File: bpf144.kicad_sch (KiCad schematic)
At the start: 39 parts

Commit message: 部品定数を入力　ただし未評価
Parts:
- C301, C330: value 10p -> NM
- C302, C329: value 10p -> 1000p
- C303, C305, C307, C309, C311, C313, C315, C317, C319, C321, C323, C325, C327: value 1p -> NM
- C304, C328: value 10p -> 47p
- C306, C320: value 10p -> 100p
- C310, C326: value 10p -> 68p
- C314: value 10p -> 22p
- C318: value 10p -> 33p
- L303, L305: value 10n -> NM
- L304, L306: value 1u -> 10n
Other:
- note added: "2t D3.5mm L3.2mm"
- note added: "Butterworth 134M-156M 26.7p, 13.1p, 98.6p"
- company: (none) -> JK1MLY / PRUG
- title: (none) -> FM QRP TRCV

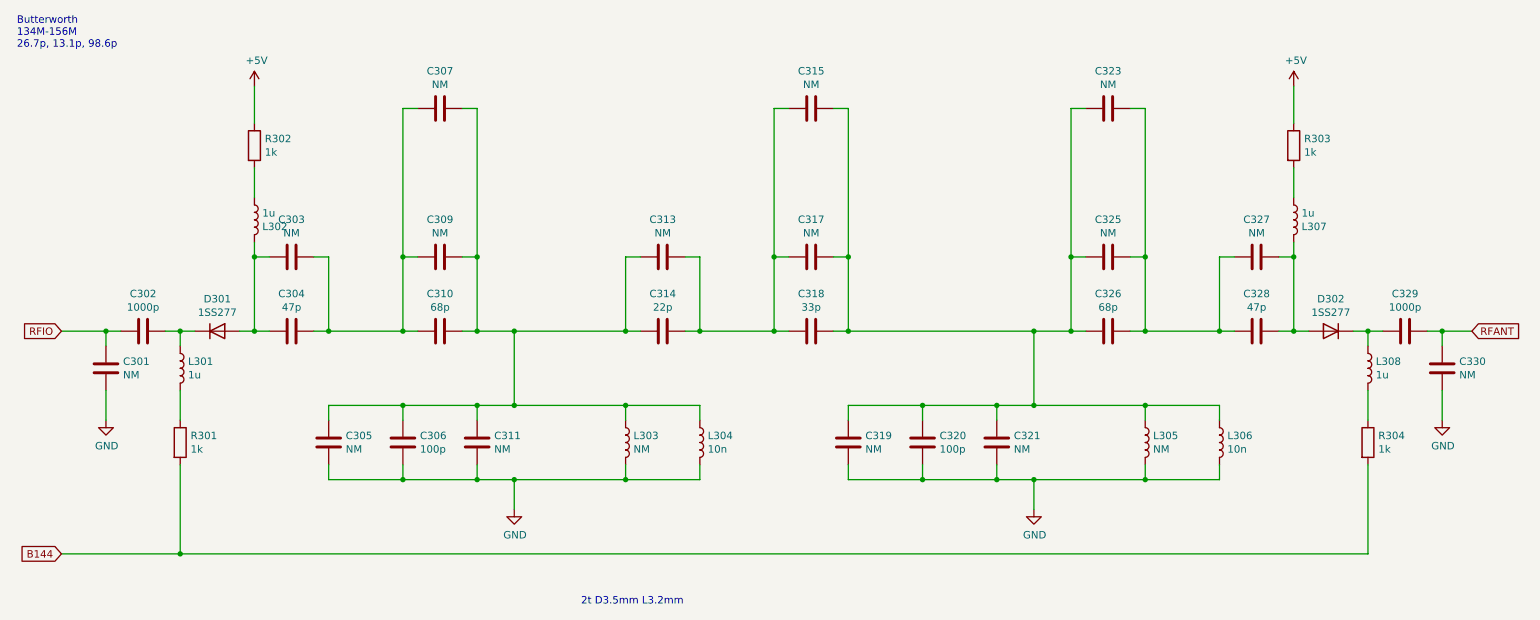
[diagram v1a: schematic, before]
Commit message: バンドパスフィルタの定数を見直し（単体試験の反映）
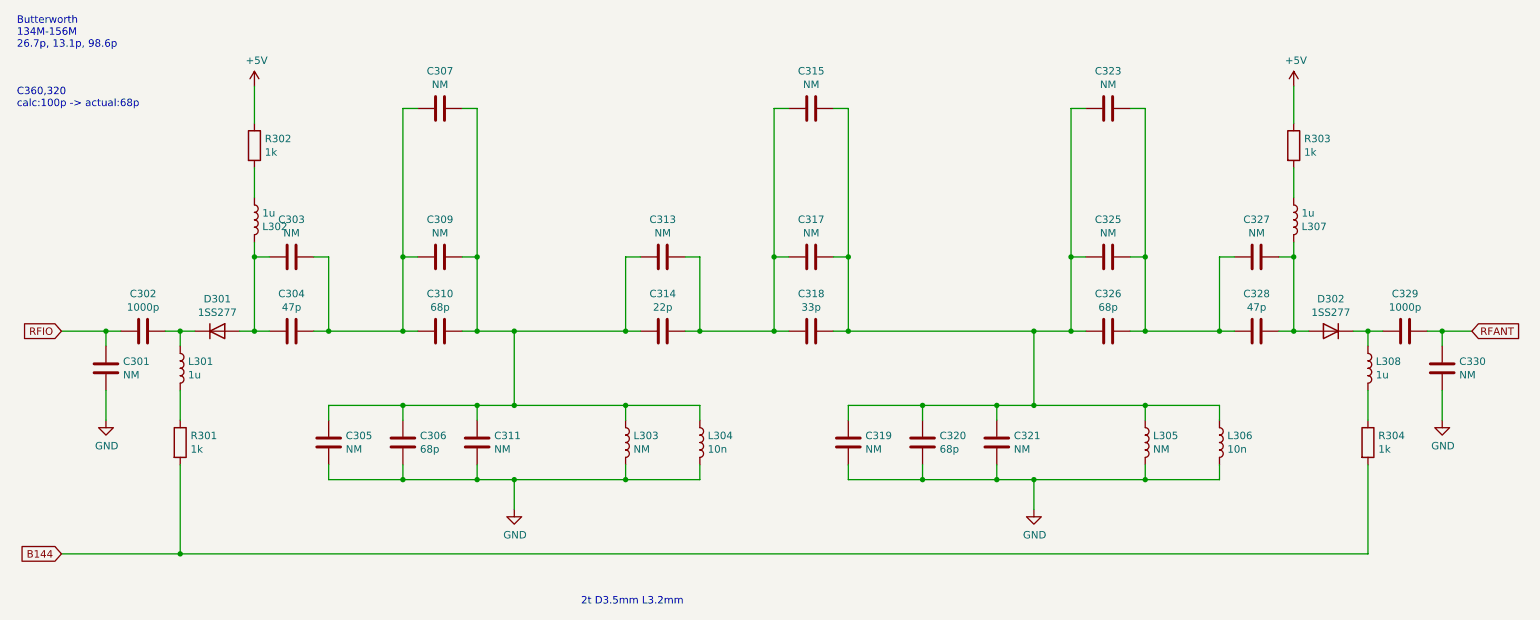
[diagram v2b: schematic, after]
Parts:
- C306, C320: value 100p -> 68p
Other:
- note added: "C360,320 calc:100p -> actual:68p"
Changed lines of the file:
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@@
+    (effects (font (size 1.27 1.27)) (justify left bottom))
+  )
+  (text "C360,320\ncalc:100p -> actual:68p" (at 22.86 38.1 0)
     (effects (font (size 1.27 1.27)) (justify left bottom))
   )
@@
       (effects (font (size 1.27 1.27)) (justify left))
     )
-    (property "Value" "100p" (id 1) (at 180.721 96.393 0)
+    (property "Value" "68p" (id 1) (at 180.721 96.393 0)
       (effects (font (size 1.27 1.27)) (justify left))
     )
@@
       (effects (font (size 1.27 1.27)) (justify left))
     )
-    (property "Value" "100p" (id 1) (at 91.821 96.393 0)
-      (effects (font (size 1.27 1.27)) (justify left))
-    )
+    (property "Value" "68p" (id 1) (at 91.821 96.393 0)
+      (effects (font (size 1.27 1.27)) (justify left))
+    )

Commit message: Add files via upload
フィルタ回路変更とジャンパクリーン
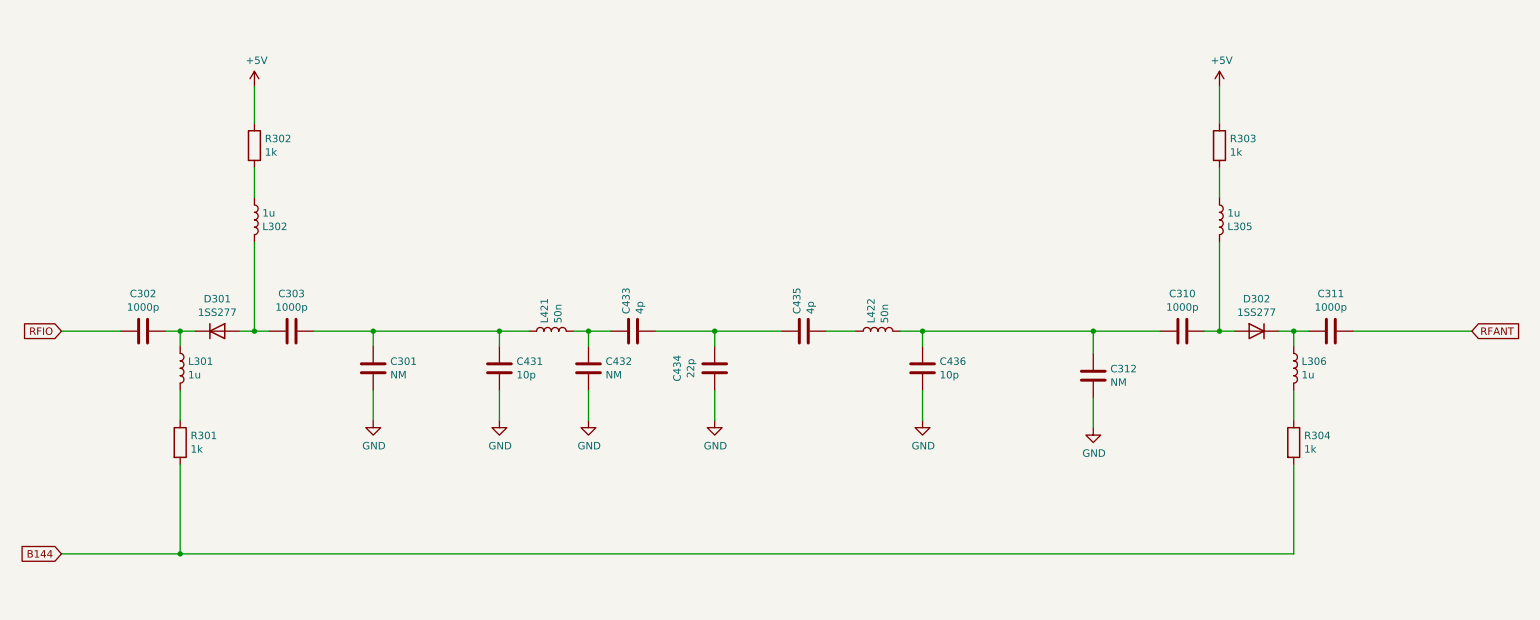
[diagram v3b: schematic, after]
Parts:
- removed C303, C305, C307, C309, C311, C313, C315, C317, C319, C321, C323, C325, C327: NM, digikey-footprints:0603, symbol Device:C
- removed C306, C310, C320, C326: 68p, Capacitor_THT:C_Disc_D3.4mm_W2.1mm_P2.50mm, symbol Device:C
- removed C314: 22p, Capacitor_THT:C_Disc_D3.4mm_W2.1mm_P2.50mm, symbol Device:C
- removed C318: 33p, Capacitor_THT:C_Disc_D3.4mm_W2.1mm_P2.50mm, symbol Device:C
- removed L303, L305: NM, Inductor_SMD:L_Murata_LQH2MCNxxxx02_2.0x1.6mm, symbol Device:L
- removed L304, L306: 10n, Resistor_THT:R_Axial_DIN0204_L3.6mm_D1.6mm_P5.08mm_Horizontal, symbol Device:L
- added C431, C436: 10p, Capacitor_THT:C_Disc_D3.4mm_W2.1mm_P2.50mm, symbol Device:C
- added C432: NM, Capacitor_THT:C_Disc_D3.4mm_W2.1mm_P2.50mm, symbol Device:C
- added C433, C435: 4p, Capacitor_THT:C_Disc_D3.4mm_W2.1mm_P2.50mm, symbol Device:C
- added C434: 22p, Capacitor_THT:C_Disc_D3.4mm_W2.1mm_P2.50mm, symbol Device:C
- added L421, L422: 50n, usr-Library:coil3_7mm, symbol Device:L
- C303: renamed from C304; value 47p -> 1000p
- C310: renamed from C328; value 47p -> 1000p
- renumbered C329 to C311, C330 to C312, L307 to L305, L308 to L306
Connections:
- net GND: now also C431.2, C432.2, C434.1, C436.2
- net RFANT: no longer C312.1
- net RFIO: no longer C301.1
- net at C303.2: now also C301.1, C431.1, L421.1
- net at C310.1: now also C312.1, C436.1, L422.2
- new net: C432.1, C433.1, L421.2
- new net: C433.2, C434.2, C435.1
- new net: C435.2, L422.1
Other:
- note removed: "2t D3.5mm L3.2mm"
- note removed: "Butterworth 134M-156M 26.7p, 13.1p, 98.6p"
- note removed: "C360,320 calc:100p -> actual:68p"
- moved on the sheet: C301, C310, C311, C312, D302, L305, L306, R303, R304

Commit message: アップデート
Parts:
- removed C301, C312: NM, Capacitor_THT:C_Disc_D3.4mm_W2.1mm_P2.50mm, symbol Device:C
- removed C435: 4p, Capacitor_THT:C_Disc_D3.4mm_W2.1mm_P2.50mm, symbol Device:C
- added R102: 1k, Resistor_THT:R_Axial_DIN0207_L6.3mm_D2.5mm_P2.54mm_Vertical, symbol Device:R
- C431, C436: value 10p -> 15p
- C432: value NM -> 15p
- C433: value 4p -> 33p
- C434: value 22p -> 15p
- D301, D302: footprint Diode_THT:D_A-405_P2.54mm_Vertical_AnodeUp -> Diode_THT:D_T-1_P5.08mm_Horizontal
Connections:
- net +5V: now also R102.1
- net B144: now also R102.2
- net at C433.2, C434.2: now also L422.1

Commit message: Add files via upload
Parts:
- C302, C303, C310, C311: value 1000p -> 0.01u
- L301, L302, L305, L306: value 1u -> 10u
- L421, L422: value 50n -> 60n
- R301, R302, R303, R304: value 1k -> 470
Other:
- note added: "L303,304は5mm 4.5T corecraft 164-04A06L相当 コアをトップと同じか半回転上にしたあたり 以前はaitendoで入手できたが現在は不可"
- note added: "注 C302 シルク無"
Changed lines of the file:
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@@
   (title_block
     (title "FM QRP TRCV")
-    (date "2022-03-12")
+    (date "2023-08-12")
     (rev "1")
     (company "JK1MLY / PRUG")
@@
   (wire (pts (xy 177.8 76.2) (xy 218.44 76.2))
     (stroke (width 0) (type default))
+  )
+  (text "注　C302 シルク無" (at 36.83 63.5 0)
+    (effects (font (size 1.27 1.27)) (justify left bottom))
+  )
+  (text "L303,304は5mm 4.5T\ncorecraft 164-04A06L相当\nコアをトップと同じか半回転上にしたあたり\n以前はaitendoで入手できたが現在は不可"
+    (at 106.68 59.69 0)
+    (effects (font (size 1.27 1.27)) (justify left bottom))
   )
   (global_label "RFANT" (shape input) (at 271.78 76.2 0) (fields_autoplaced)
@@
       (effects (font (size 1.27 1.27)) (justify left))
     )
-    (property "Value" "1u" (at 242.6462 83.693 0)
+    (property "Value" "10u" (at 242.6462 83.693 0)
       (effects (font (size 1.27 1.27)) (justify left))
     )
@@
       (effects (font (size 1.27 1.27)) (justify left))
     )
-    (property "Value" "1k" (at 65.278 45.593 0)
+    (property "Value" "470" (at 65.278 45.593 0)
       (effects (font (size 1.27 1.27)) (justify left))
     )
@@
       (effects (font (size 1.27 1.27)) hide)
     )
-    (property "Datasheet" "~" (at 63.5 44.45 0)
+    (property "Datasheet" "R-25471" (at 63.5 44.45 0)
       (effects (font (size 1.27 1.27)) hide)
     )
@@
       (effects (font (size 1.27 1.27)) (justify left))
     )
-    (property "Value" "1k" (at 243.078 96.393 0)
+    (property "Value" "470" (at 243.078 96.393 0)
       (effects (font (size 1.27 1.27)) (justify left))
     )
@@
       (effects (font (size 1.27 1.27)) hide)
     )
-    (property "Datasheet" "~" (at 241.3 95.25 0)
+    (property "Datasheet" "R-25471" (at 241.3 95.25 0)
       (effects (font (size 1.27 1.27)) hide)
     )
@@
       (effects (font (size 1.27 1.27)))
     )
-    (property "Value" "1000p" (at 69.85 72.1106 90)
+    (property "Value" "0.01u" (at 69.85 72.1106 90)
       (effects (font (size 1.27 1.27)))
     )
@@
       (effects (font (size 1.27 1.27)) hide)
     )
-    (property "Datasheet" "~" (at 69.85 76.2 0)
+    (property "Datasheet" "sato" (at 69.85 76.2 0)
       (effects (font (size 1.27 1.27)) hide)
     )
@@
       (effects (font (size 1.27 1.27)))
     )
-    (property "Value" "1000p" (at 222.25 72.1106 90)
+    (property "Value" "0.01u" (at 222.25 72.1106 90)
       (effects (font (size 1.27 1.27)))
     )
@@
       (effects (font (size 1.27 1.27)) hide)
     )
-    (property "Datasheet" "~" (at 222.25 76.2 0)
+    (property "Datasheet" "sato" (at 222.25 76.2 0)
       (effects (font (size 1.27 1.27)) hide)
     )
@@
       (effects (font (size 1.27 1.27)) (justify left))
     )
-    (property "Value" "1u" (at 52.1462 83.693 0)
+    (property "Value" "10u" (at 52.1462 83.693 0)
       (effects (font (size 1.27 1.27)) (justify left))
     )
@@
       (effects (font (size 1.27 1.27)) (justify left))
     )
-    (property "Value" "1k" (at 52.578 96.393 0)
+    (property "Value" "470" (at 52.578 96.393 0)
       (effects (font (size 1.27 1.27)) (justify left))
     )
@@
       (effects (font (size 1.27 1.27)) hide)
     )
-    (property "Datasheet" "~" (at 50.8 95.25 0)
+    (property "Datasheet" "R-25471" (at 50.8 95.25 0)
       (effects (font (size 1.27 1.27)) hide)
     )
@@
       (effects (font (size 1.27 1.27)) (justify left))
     )
-    (property "Value" "1u" (at 64.8462 56.007 0)
+    (property "Value" "10u" (at 64.8462 56.007 0)
       (effects (font (size 1.27 1.27)) (justify left))
     )
@@
       (effects (font (size 1.27 1.27)) (justify left))
     )
-    (property "Value" "1k" (at 230.378 45.593 0)
+    (property "Value" "470" (at 230.378 45.593 0)
       (effects (font (size 1.27 1.27)) (justify left))
     )
@@
       (effects (font (size 1.27 1.27)) hide)
     )
-    (property "Datasheet" "~" (at 228.6 44.45 0)
+    (property "Datasheet" "R-25471" (at 228.6 44.45 0)
       (effects (font (size 1.27 1.27)) hide)
     )
@@
       (effects (font (size 1.27 1.27)) (justify left))
     )
-    (property "Value" "1u" (at 229.9462 56.007 0)
+    (property "Value" "10u" (at 229.9462 56.007 0)
       (effects (font (size 1.27 1.27)) (justify left))
     )
@@
       (effects (font (size 1.27 1.27)))
     )
-    (property "Value" "1000p" (at 247.65 72.1106 90)
+    (property "Value" "0.01u" (at 247.65 72.1106 90)
       (effects (font (size 1.27 1.27)))
     )
@@
       (effects (font (size 1.27 1.27)) hide)
     )
-    (property "Datasheet" "~" (at 247.65 76.2 0)
+    (property "Datasheet" "sato" (at 247.65 76.2 0)
       (effects (font (size 1.27 1.27)) hide)
     )
@@
       (effects (font (size 1.27 1.27)))
     )
-    (property "Value" "1000p" (at 44.45 72.1106 90)
+    (property "Value" "0.01u" (at 44.45 72.1106 90)
       (effects (font (size 1.27 1.27)))
     )
@@
       (effects (font (size 1.27 1.27)) hide)
     )
-    (property "Datasheet" "~" (at 44.45 76.2 0)
+    (property "Datasheet" "sato" (at 44.45 76.2 0)
       (effects (font (size 1.27 1.27)) hide)
     )
@@
       (effects (font (size 1.27 1.27)) (justify left))
     )
-    (property "Value" "50n" (at 115.443 74.8538 0)
+    (property "Value" "60n" (at 115.443 74.8538 0)
       (effects (font (size 1.27 1.27)) (justify left))
     )
@@
       (effects (font (size 1.27 1.27)) hide)
     )
-    (property "Datasheet" "digikey 0805CS-3N3EJTS" (at 114.3 76.2 0)
+    (property "Datasheet" "aitendo" (at 114.3 76.2 0)
       (effects (font (size 1.27 1.27)) hide)
     )
@@
       (effects (font (size 1.27 1.27)) hide)
     )
-    (property "Datasheet" "~" (at 105.41 82.55 0)
+    (property "Datasheet" "sato" (at 105.41 82.55 0)
       (effects (font (size 1.27 1.27)) hide)
     )
@@
       (effects (font (size 1.27 1.27)) hide)
     )
-    (property "Datasheet" "~" (at 177.8 82.55 0)
+    (property "Datasheet" "sato" (at 177.8 82.55 0)
       (effects (font (size 1.27 1.27)) hide)
     )
@@
       (effects (font (size 1.27 1.27)) hide)
     )
-    (property "Datasheet" "~" (at 128.27 76.2 0)
+    (property "Datasheet" "sato" (at 128.27 76.2 0)
       (effects (font (size 1.27 1.27)) hide)
     )
@@
       (effects (font (size 1.27 1.27)) hide)
     )
-    (property "Datasheet" "~" (at 120.65 82.55 0)
+    (property "Datasheet" "sato" (at 120.65 82.55 0)
       (effects (font (size 1.27 1.27)) hide)
     )
@@
       (effects (font (size 1.27 1.27)) hide)
     )
-    (property "Datasheet" "~" (at 142.24 82.55 0)
+    (property "Datasheet" "sato" (at 142.24 82.55 0)
       (effects (font (size 1.27 1.27)) hide)
     )
@@
       (effects (font (size 1.27 1.27)) hide)
     )
-    (property "Datasheet" "~" (at 39.37 104.14 0)
+    (property "Datasheet" "R-25102" (at 39.37 104.14 0)
       (effects (font (size 1.27 1.27)) hide)
     )
@@
       (effects (font (size 1.27 1.27)) (justify left))
     )
-    (property "Value" "50n" (at 171.323 74.8538 0)
+    (property "Value" "60n" (at 171.323 74.8538 0)
       (effects (font (size 1.27 1.27)) (justify left))
     )
@@
       (effects (font (size 1.27 1.27)) hide)
     )
-    (property "Datasheet" "digikey 0805CS-3N3EJTS" (at 170.18 76.2 0)
-      (effects (font (size 1.27 1.27)) hide)
-    )
+    (property "Datasheet" "aitendo" (at 170.18 76.2 0)
+      (effects (font (size 1.27 1.27)) hide)
+    )
